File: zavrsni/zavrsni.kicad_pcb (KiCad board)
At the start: 2 copper layers, 48 parts, among them Q1 BC337, Q2 PNP, SW1 RotaryEncoder_Switch, SW2 SW_Push_DPDT, U1 PCM3060, U2 WeAct STM32F411CEU6 v3.0, U3 NE5532, U4 TL074, U5 LM358, U6 LM317_TO-220, U7 UC1609C LCD Board

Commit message: PCB design, implement basic DAC/ADC
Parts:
- removed C16: 10u, Capacitor_THT:CP_Radial_D5.0mm_P2.50mm
- removed C17: 100n, Capacitor_THT:C_Disc_D5.0mm_W2.5mm_P5.00mm
- removed SW2: SW_Push_DPDT, Button_Switch_THT:SW_Push_2P2T_Toggle_CK_PVA2xxH2xxxxxxV2
- added C18: 100n, Capacitor_THT:C_Disc_D5.0mm_W2.5mm_P5.00mm, F.Cu at (73.5, 86.0)
- added C19: 10u, Capacitor_THT:CP_Radial_D5.0mm_P2.50mm, F.Cu at (70.2, 87.0)
- added C20: 100u, Capacitor_THT:CP_Radial_D5.0mm_P2.50mm, F.Cu at (72.5, 83.2)
- added C21: 100n, Capacitor_THT:C_Disc_D5.0mm_W2.5mm_P5.00mm, F.Cu at (135.3, 108.2)
- added C22: 10u, Capacitor_THT:CP_Radial_D5.0mm_P2.50mm, F.Cu at (135.4, 91.2)
- added C23: 10u, Capacitor_THT:CP_Radial_D5.0mm_P2.50mm, F.Cu at (124.9, 70.0)
- added C24: 10u, Capacitor_THT:CP_Radial_D5.0mm_P2.50mm, F.Cu at (120.1, 95.3)
- added Jout1: Conn_01x01_Pin, Connector_Wire:SolderWirePad_1x01_SMD_4x8mm, F.Cu at (230.6, 112.3)
- added Jvcc1: Conn_01x01_Pin, Connector_Wire:SolderWirePad_1x01_SMD_4x8mm, F.Cu at (118.6, 91.0)
- added Jvss1: Conn_01x01_Pin, Connector_Wire:SolderWirePad_1x01_SMD_4x8mm, F.Cu at (146.0, 100.3)
- added SW_PRESET_0: SW_Push, Button_Switch_THT:SW_PUSH_6mm_H13mm, F.Cu at (55.0, 20.0)
- added SW_PRESET_1: SW_Push, Button_Switch_THT:SW_PUSH_6mm_H13mm, F.Cu at (55.0, 45.0)
- added SW_PRESET_2: SW_Push, Button_Switch_THT:SW_PUSH_6mm_H13mm, F.Cu at (55.0, 70.0)
- added SW_PRESET_3: SW_Push, Button_Switch_THT:SW_PUSH_6mm_H13mm, F.Cu at (55.0, 95.0)
- added SW_PRESET_4: SW_Push, Button_Switch_THT:SW_PUSH_6mm_H13mm, F.Cu at (30.0, 20.0)
- added SW_PRESET_5: SW_Push, Button_Switch_THT:SW_PUSH_6mm_H13mm, F.Cu at (30.0, 45.0)
- added SW_PRESET_6: SW_Push, Button_Switch_THT:SW_PUSH_6mm_H13mm, F.Cu at (30.0, 70.0)
- added SW_PRESET_7: SW_Push, Button_Switch_THT:SW_PUSH_6mm_H13mm, F.Cu at (30.0, 95.0)
- C12, C3: value 10u -> 100n; footprint Capacitor_THT:CP_Radial_D5.0mm_P2.50mm -> Capacitor_THT:C_Disc_D5.0mm_W2.5mm_P5.00mm
- C4: value 100n -> 10u; footprint Capacitor_THT:C_Disc_D5.0mm_W2.5mm_P5.00mm -> Capacitor_THT:CP_Radial_D5.0mm_P2.50mm
- Jin1: footprint Connector_Wire:SolderWirePad_1x01_SMD_3x6mm -> Connector_Wire:SolderWirePad_1x01_SMD_4x8mm
- Q2: value PNP -> BC317
- SW1: value RotaryEncoder_Switch -> EC11_SW; footprint Rotary_Encoder:RotaryEncoder_Alps_EC11E-Switch_Vertical_H20mm_CircularMountingHoles -> ljepi:ec11
- U1: value PCM3060 -> CS4335; footprint Package_DIP:DIP-28_W15.24mm_Socket -> Package_SO:SOIC-8_3.9x4.9mm_P1.27mm
- moved C13 155.9 mm to (264.0, 41.0)
- moved U1 147.3 mm to (270.2, 60.7)
- moved C3 138.5 mm to (254.7, 66.8)
- moved C12 138.4 mm to (254.7, 83.0)
- moved SW1 122.7 mm to (245.4, 110.3)
- moved C4 107.0 mm to (257.3, 47.5)
- moved C14 106.6 mm to (53.9, 122.8)
- moved C9 103.3 mm to (247.1, 88.6)
- moved U7 87.6 mm to (77.8, 125.0)
- moved U6 69.1 mm to (90.5, 92.5)
- moved U4 66.6 mm to (99.0, 80.5), turned to 90 degrees
- moved R3 65.1 mm to (138.6, 105.7), turned to 90 degrees
- moved R1 64.6 mm to (144.5, 84.0), turned to 90 degrees
- moved R4 62.0 mm to (141.9, 95.5), turned to -90 degrees
- moved R2 56.5 mm to (138.6, 56.9), turned to -90 degrees
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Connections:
- net IN renamed /IN
- net Net-(U2-A5) renamed /LCD_SCK
- net Net-(U2-A7) renamed /LCD_SDA
- net Net-(U2-B0) renamed /LCD_CS
- net Net-(U2-B1) renamed /LCD_CD
- C12 pad 1: +5V -> /LCD_VCC
- C13 pad 1: +3V3 -> /LCD_VCC
- C14 pad 1: GNDREF -> +12V
- C14 pad 2: +3V3 -> GNDREF
- C15 pad 1: GNDREF -> Net-(U4B-+)
- C15 pad 2: +5V -> GNDREF
- C3 pad 1: +12V -> +5V
- C3 pad 2: +0V -> GNDREF
- C4 pad 1: +12V -> +5V
- C4 pad 2: +0V -> GNDREF
- R10 pad 1: Net-(U4A-+) -> Net-(U4B-+)
- R11 pad 2: Net-(U4A-+) -> Net-(U4B-+)
- R12 pad 1: Net-(U4A--) -> Net-(U4B--)
- R13 pad 2: Net-(U4A--) -> Net-(U4B--)
- SW1 pad A: unconnected-(SW1-PadA) -> /ROT_A
- SW1 pad B: unconnected-(SW1-PadB) -> /ROT_B
- SW1 pad C: unconnected-(SW1-PadC) -> GNDREF
- SW1 pad MP: (no net) -> GNDREF
- SW1 pad S1: unconnected-(SW1-PadS1) -> /ROT_SW
- SW1 pad S2: unconnected-(SW1-PadS2) -> GNDREF
- U1 pad 1: unconnected-(U1-MC/SCL/FMT-Pad1) -> /DAC_DAT
- U1 pad 2: unconnected-(U1-MD/SDA/DEMP-Pad2) -> /DAC_BCLK
- U1 pad 3: unconnected-(U1-DOUT-Pad3) -> /DAC_LRCLK
- U1 pad 4: unconnected-(U1-LRCK1-Pad4) -> /DAC_MCLK
- U1 pad 5: unconnected-(U1-BCK1-Pad5) -> /OUT
- U1 pad 6: unconnected-(U1-SCKI1-Pad6) -> GNDREF
- U1 pad 7: +3V3 -> +5V
- U1 pad 8: GNDREF -> unconnected-(U1-AOUTL-Pad8)
- U2 pad 1: unconnected-(U2-B12-Pad1) -> /DAC_LRCLK
- U2 pad 10: unconnected-(U2-A15-Pad10) -> /PRESET6
- U2 pad 11: unconnected-(U2-B3-Pad11) -> /PRESET5
- U2 pad 12: unconnected-(U2-B4-Pad12) -> /PRESET4
- U2 pad 13: unconnected-(U2-B5-Pad13) -> /PRESET3
- U2 pad 14: unconnected-(U2-B6-Pad14) -> /PRESET2
- U2 pad 15: unconnected-(U2-B7-Pad15) -> /PRESET1
- U2 pad 17: unconnected-(U2-B9-Pad17) -> /PRESET0
- U2 pad 18: unconnected-(U2-5V-Pad18) -> +5V
- U2 pad 19: unconnected-(U2-GND-Pad19) -> GNDREF
- U2 pad 2: unconnected-(U2-B13-Pad2) -> /ROT_B
- U2 pad 20: unconnected-(U2-3V3-Pad20) -> +3V3
- U2 pad 26: unconnected-(U2-A0-Pad26) -> /ADC_IN
- U2 pad 29: unconnected-(U2-A3-Pad29) -> /DAC_MCLK
- U2 pad 3: unconnected-(U2-B14-Pad3) -> /ROT_A
- U2 pad 32: unconnected-(U2-A6-Pad32) -> /LCD_RST
- U2 pad 36: Net-(U2-B2) -> /LCD_VCC
- U2 pad 37: Net-(U2-B10) -> /DAC_BCLK
- U2 pad 39: unconnected-(U2-GND-Pad39) -> GNDREF
- U2 pad 4: unconnected-(U2-B15-Pad4) -> /DAC_DAT
- U2 pad 5: unconnected-(U2-A8-Pad5) -> /ROT_SW
- U2 pad 9: unconnected-(U2-A12-Pad9) -> /PRESET7
- U4 pad 1: Net-(R13-Pad1) -> Net-(D2-A)
- U4 pad 10: +5V -> GNDREF
- U4 pad 13: Net-(U1-V_{IN}L) -> /ADC_IN
- U4 pad 14: Net-(U1-V_{IN}L) -> /ADC_IN
- U4 pad 2: Net-(U4A--) -> Net-(D1-A)
- U4 pad 3: Net-(U4A-+) -> +5V
- U4 pad 5: GNDREF -> Net-(U4B-+)
- U4 pad 6: Net-(D1-A) -> Net-(U4B--)
- U4 pad 7: Net-(D1-K) -> Net-(R13-Pad1)
- U4 pad 8: Net-(D2-A) -> Net-(D1-K)
- U7 pad 4: Net-(U2-B2) -> /LCD_VCC
- U7 pad 7: Net-(U2-B10) -> /LCD_RST
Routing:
- net +0V: track 0.00 -> 111.9 mm, vias 0 -> 2
- net +12V: track 0.00 -> 80.6 mm
- net +5V: track 0.00 -> 41.8 mm
- net Net-(D1-A): track 0.00 -> 37.4 mm
- net Net-(U4B--): track 0.00 -> 17.8 mm
- net Net-(U5A-+): track 0.00 -> 17.5 mm
- net Net-(U3B-+): track 0.00 -> 16.4 mm
- net Net-(Q1-B): track 0.00 -> 15.4 mm
- net Net-(U6-ADJ): track 0.00 -> 12.2 mm
- net GNDREF: track 0.00 -> 11.5 mm, vias 0 -> 4
- net Net-(U3B--): track 0.00 -> 11.1 mm
- net Net-(U4B-+): track 0.00 -> 11.1 mm
- net +3V3: track 0.00 -> 10.5 mm
- net /ADC_IN: track 0.00 -> 9.32 mm
- net Net-(R13-Pad1): track 0.00 -> 8.47 mm
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- added copper zone on F.Cu, net +0V
- added copper zone on F.Cu, net +12V
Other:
- board outline added: 228.6 x 139.7 mm

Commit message: PCB is done
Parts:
- removed SW1: EC11_SW, ljepi:ec11
- removed SW_PRESET_7: SW_Push, Button_Switch_THT:SW_PUSH_6mm_H13mm
- U6: footprint Package_TO_SOT_THT:TO-220-3_Vertical -> Package_TO_SOT_THT:TO-220-3_Horizontal_TabDown
- moved C9 190.9 mm to (56.7, 101.4), turned to -90 degrees
- moved SW_UP1 173.0 mm to (184.4, 98.0), turned to 90 degrees
- moved SW_DOWN1 168.8 mm to (184.4, 113.0), turned to 90 degrees
- moved C13 165.2 mm to (107.5, 93.9), turned to 90 degrees
- moved U1 155.1 mm to (115.1, 60.5), turned to 90 degrees
- moved SW_OK1 154.5 mm to (184.4, 72.0), turned to 90 degrees
- moved C4 151.6 mm to (106.5, 62.4), turned to 90 degrees
- moved C12 150.6 mm to (104.2, 88.4)
- moved C3 144.0 mm to (110.8, 62.2), turned to 90 degrees
- moved SW_PRESET_3 135.7 mm to (184.7, 134.8), turned to 90 degrees
- moved SW_PRESET_2 125.2 mm to (162.1, 134.8), turned to 90 degrees
- moved SW_PRESET_0 124.1 mm to (102.1, 134.8), turned to 90 degrees
- moved Jout1 123.1 mm to (120.2, 57.9)
- moved SW_PRESET_1 118.4 mm to (132.1, 134.8), turned to 90 degrees
- moved Jvss1 97.5 mm to (55.0, 135.3), turned to -90 degrees
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- renumbered SW_PRESET_5 to SW_DOWN1, SW_PRESET_6 to SW_OK1, SW_PRESET_4 to SW_UP1
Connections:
- net /PRESET0 renamed /BTN_PRESET0
- net /PRESET1 renamed /BTN_PRESET1
- net /PRESET2 renamed /BTN_PRESET2
- net /PRESET3 renamed /BTN_PRESET3
- net /PRESET6 renamed /BTN_OK
- SW_DOWN1 pad 1: /PRESET5 -> /BTN_DOWN
- SW_UP1 pad 1: /PRESET4 -> /BTN_UP
- U2 pad 11: /PRESET5 -> /BTN_UP
- U2 pad 12: /PRESET4 -> /BTN_DOWN
- U2 pad 2: /ROT_B -> /DAC_BCLK
- U2 pad 3: /ROT_A -> unconnected-(U2-B14-Pad3)
- U2 pad 37: /DAC_BCLK -> unconnected-(U2-B10-Pad37)
- U2 pad 38: unconnected-(U2-3V3-Pad38) -> +3V3
- U2 pad 5: /ROT_SW -> unconnected-(U2-A8-Pad5)
- U2 pad 9: /PRESET7 -> unconnected-(U2-A12-Pad9)
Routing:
- net /BTN_PRESET3: track 0.00 -> 145.4 mm
- net /BTN_PRESET2: track 0.00 -> 125.7 mm
- net /BTN_DOWN: track 0.00 -> 117.2 mm
- net /BTN_PRESET0: track 0.00 -> 115.8 mm
- net /BTN_UP: track 0.00 -> 108.2 mm
- net /BTN_PRESET1: track 0.00 -> 99.3 mm
- net /BTN_OK: track 0.00 -> 91.8 mm
- net /LCD_SCK: track 0.00 -> 68.2 mm
- net +5V: track 41.8 -> 97.5 mm
- net /LCD_SDA: track 0.00 -> 54.9 mm
- net /DAC_MCLK: track 0.00 -> 46.1 mm, vias 0 -> 1
- net /LCD_RST: track 0.00 -> 35.2 mm, vias 0 -> 2
- net /LCD_CS: track 0.00 -> 34.0 mm
- net /LCD_CD: track 0.00 -> 30.0 mm
- net +12V: track 80.6 -> 107.6 mm
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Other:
- board size 228.6 x 139.7 mm -> 156.4 x 99.2 mm
- board text added: "${CRTAO} Pedala multiefekata za električnu gitaru ${DATUM} v${VERZIJA}"

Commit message: PCB prototype finishing touches
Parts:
- removed C10: 100n, Capacitor_THT:C_Disc_D5.0mm_W2.5mm_P5.00mm
- removed C23: 10u, Capacitor_THT:CP_Radial_D5.0mm_P2.50mm
- removed R5: 1k, Resistor_THT:R_Axial_DIN0207_L6.3mm_D2.5mm_P10.16mm_Horizontal
- added RV1: R_Potentiometer_MountingPin, ljepi:pot vertikalni 5 pin, F.Cu at (70.9, 120.9)
- added SW_TUNER1: SW_Push, Button_Switch_THT:SW_PUSH_6mm_H13mm, F.Cu at (95.2, 116.0)
- D1, D2: footprint Diode_THT:D_DO-35_SOD27_P7.62mm_Horizontal -> Diode_THT:D_DO-35_SOD27_P2.54mm_Vertical_AnodeUp
- Q2: value BC317 -> BC327
- R1, R10, R12, R9: footprint Resistor_THT:R_Axial_DIN0207_L6.3mm_D2.5mm_P10.16mm_Horizontal -> Resistor_THT:R_Axial_DIN0207_L6.3mm_D2.5mm_P5.08mm_Vertical
- R11, R13, R2, R7, R8: footprint Resistor_THT:R_Axial_DIN0207_L6.3mm_D2.5mm_P10.16mm_Horizontal -> Resistor_THT:R_Axial_DIN0207_L6.3mm_D2.5mm_P2.54mm_Vertical
- R6: value 330 -> 300; footprint Resistor_THT:R_Axial_DIN0207_L6.3mm_D2.5mm_P10.16mm_Horizontal -> Resistor_THT:R_Axial_DIN0207_L6.3mm_D2.5mm_P2.54mm_Vertical
- moved SW_UP1 65.7 mm to (121.2, 116.0), turned to -90 degrees
- moved SW_OK1 52.9 mm to (168.8, 122.5)
- moved SW_DOWN1 42.8 mm to (142.8, 122.5)
- moved SW_PRESET_2 19.6 mm to (142.8, 138.2)
- moved SW_PRESET_3 16.3 mm to (168.8, 138.2)
- moved C7 15.5 mm to (82.6, 120.9)
- moved SW_PRESET_1 11.3 mm to (121.2, 131.8), turned to -90 degrees
- moved R7 9.25 mm to (55.8, 91.5)
- moved D1 9.20 mm to (85.2, 103.6), turned to 90 degrees
- moved R6 9.01 mm to (75.6, 123.7)
- moved R2 8.92 mm to (82.0, 142.2), turned to 0 degrees
- moved C1 8.85 mm to (78.9, 140.5), turned to -90 degrees
- moved C2 7.83 mm to (81.7, 137.9), turned to 0 degrees
- moved SW_PRESET_0 7.50 mm to (95.2, 131.8), turned to -90 degrees
- moved R12 7.39 mm to (81.5, 109.7), turned to -90 degrees
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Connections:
- Q2 pad 1: GNDREF -> +0V
- Q2 pad 3: +0V -> GNDREF
- U2 pad 11: /BTN_UP -> /BTN_DOWN
- U2 pad 12: /BTN_DOWN -> /BTN_PRESET3
- U2 pad 13: /BTN_PRESET3 -> /BTN_PRESET2
- U2 pad 14: /BTN_PRESET2 -> /BTN_PRESET1
- U2 pad 15: /BTN_PRESET1 -> /BTN_PRESET0
- U2 pad 16: unconnected-(U2-B8-Pad16) -> /BTN_UP
- U2 pad 17: /BTN_PRESET0 -> /BTN_TUNER
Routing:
- net /BTN_TUNER: track 0.00 -> 121.6 mm, vias 0 -> 2
- net +12V: track 107.6 -> 79.6 mm
- net /BTN_DOWN: track 117.2 -> 91.1 mm, vias 0 -> 2
- net GNDREF: track 27.0 -> 4.06 mm, vias 6 -> 2
- net /BTN_OK: track 91.8 -> 114.5 mm, vias 0 -> 2
- net /BTN_PRESET0: track 115.8 -> 137.2 mm, vias 0 -> 2
- net Net-(C7-Pad1): track 7.10 -> 21.1 mm
- net /BTN_PRESET2: track 125.7 -> 111.8 mm, vias 0 -> 2
- net /BTN_UP: track 108.2 -> 95.6 mm, vias 0 -> 2
- net /BTN_PRESET1: track 99.3 -> 111.1 mm, vias 0 -> 2
- net /BTN_PRESET3: track 145.4 -> 135.3 mm, vias 0 -> 2
- net Net-(D1-K): track 8.14 -> 2.84 mm
- net Net-(U3B--): track 11.6 -> 7.88 mm
- net Net-(U3B-+): track 17.9 -> 20.8 mm
- net /OUT: track 3.96 -> 6.33 mm
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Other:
- board size 156.4 x 99.2 mm -> 149.4 x 96.2 mm
- board text added: "${CRTAO} Mutliefekt pedala za električnu gitaru ${DATUM} v${VERZIJA}"
- board text removed: "${CRTAO} Pedala multiefekata za električnu gitaru ${DATUM} v${VERZIJA}"

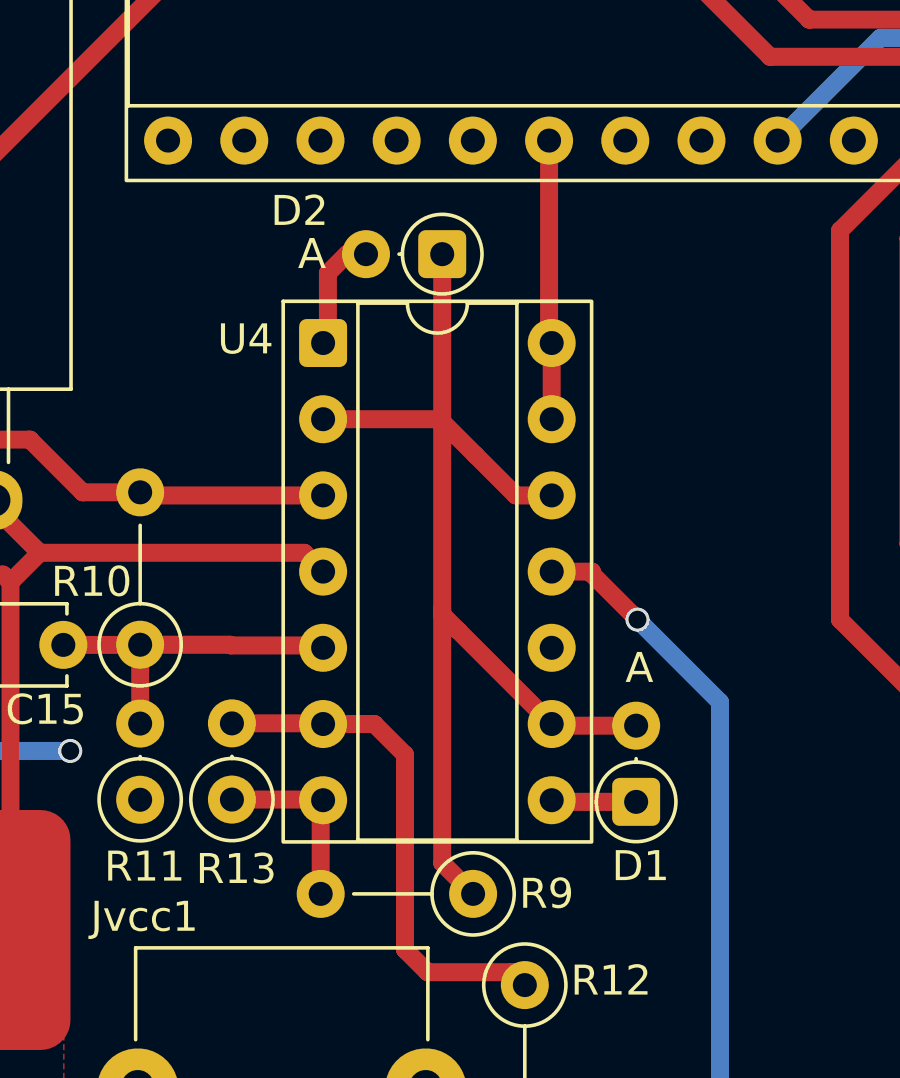
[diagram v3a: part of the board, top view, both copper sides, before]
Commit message: izbrisi svg pdfove, zamjeni polaritet 2 diode
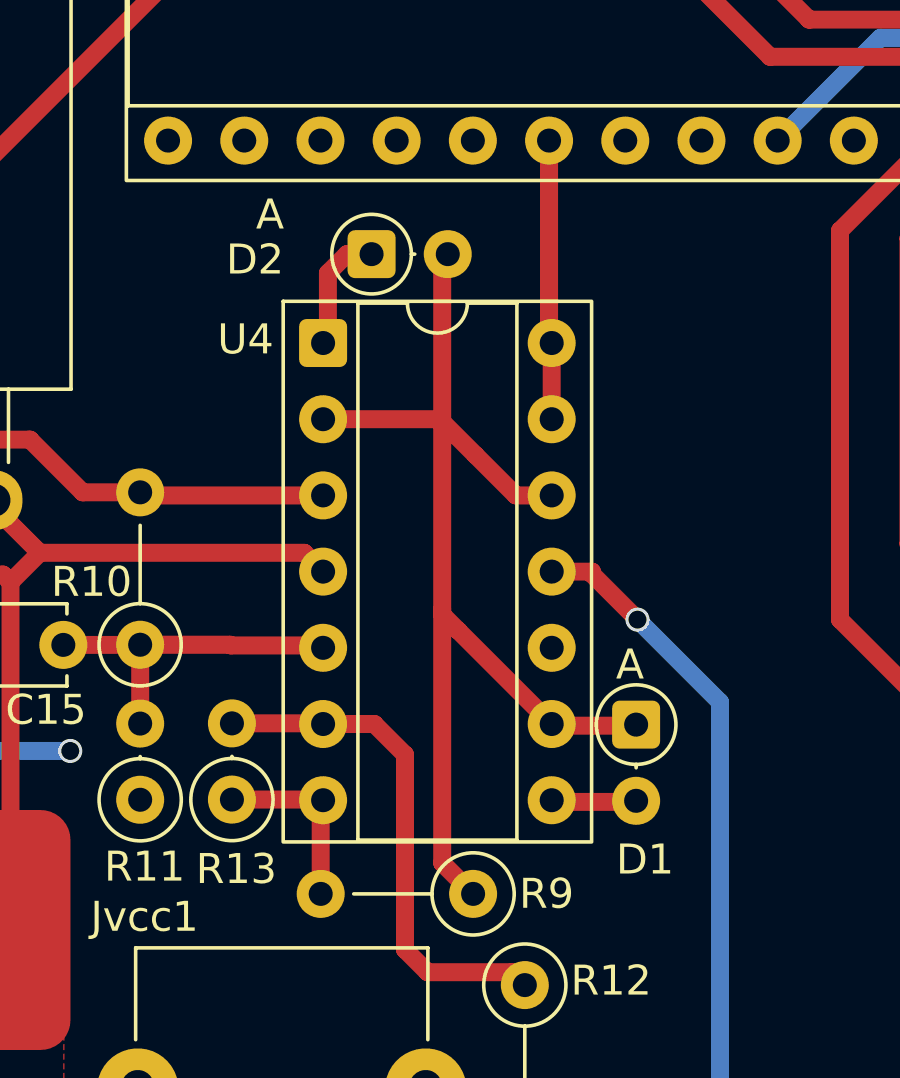
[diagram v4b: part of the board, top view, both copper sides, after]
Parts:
- moved D1 2.58 mm to (85.2, 101.0), turned to -90 degrees
- moved D2 2.35 mm to (76.4, 85.3), turned to 0 degrees
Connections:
- D2 pad 1: Net-(D1-A) -> Net-(D2-K)
- D2 pad 2: Net-(D2-A) -> Net-(D1-K)
- R9 pad 1: Net-(D1-A) -> Net-(D1-K)
- U4 pad 1: Net-(D2-A) -> Net-(D2-K)
- U4 pad 12: Net-(D1-A) -> Net-(D1-K)
- U4 pad 2: Net-(D1-A) -> Net-(D1-K)
- U4 pad 8: Net-(D1-K) -> Net-(D1-A)
- U4 pad 9: Net-(D1-A) -> Net-(D1-K)
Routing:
- net Net-(D1-K): track 2.84 -> 38.9 mm
- net Net-(D1-A): track 38.9 -> 2.84 mm
- net Net-(D2-K): track 0.00 -> 3.93 mm
- net Net-(D2-A): track 3.93 -> 0.00 mm
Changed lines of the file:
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@@
 	(net 28 "Net-(D1-K)")
 	(net 29 "Net-(D1-A)")
-	(net 30 "Net-(D2-A)")
+	(net 30 "Net-(D2-K)")
 	(net 31 "Net-(Q1-B)")
 	(net 32 "Net-(U3A--)")
@@
 	(footprint "Diode_THT:D_DO-35_SOD27_P2.54mm_Vertical_AnodeUp"
 		(layer "F.Cu")
-		(at 85.204646 103.575538 90)
+		(at 85.204646 101 -90)
 		(descr "Diode, DO-35_SOD27 series, Axial, Vertical, pin pitch=2.54mm, length*diameter=4*2mm^2, http://www.diodes.com/_files/packages/DO-35.pdf")
 		(tags "Diode DO-35_SOD27 series Axial Vertical pin pitch 2.54mm  length 4mm diameter 2mm")
 		(property "Reference" "D1"
-			(at -2.145133 0.152333 180)
+			(at 4.5 -0.295354 0)
 			(layer "F.SilkS")
 			(effects
@@
 		)
 		(property "Sim.Device" "D"
-			(at 0 0 90)
+			(at 0 0 270)
 			(unlocked yes)
 			(layer "F.Fab")
@@
 		)
 		(property "Sim.Pins" "1=K 2=A"
-			(at 0 0 90)
+			(at 0 0 270)
 			(unlocked yes)
 			(layer "F.Fab")
@@
 		)
 		(fp_text user "A"
-			(at 4.460235 0.109066 180)
+			(at -2 0.204646 0)
 			(layer "F.SilkS")
 			(effects
@@
 		)
 		(pad "1" thru_hole roundrect
-			(at 0 0 90)
+			(at 0 0 270)
 			(size 1.6 1.6)
 			(drill 0.8)
@@
 		)
 		(pad "2" thru_hole circle
-			(at 2.54 0 90)
+			(at 2.54 0 270)
 			(size 1.6 1.6)
 			(drill 0.8)
@@
 			(remove_unused_layers no)
 			(roundrect_rratio 0.15625)
-			(net 30 "Net-(D2-A)")
+			(net 30 "Net-(D2-K)")
 			(pintype "output")
 		)
@@
 			(layers "*.Cu" "*.Mask")
 			(remove_unused_layers no)
-			(net 29 "Net-(D1-A)")
+			(net 28 "Net-(D1-K)")
 			(pinfunction "-")
 			(pintype "input")
@@
 			(layers "*.Cu" "*.Mask")
 			(remove_unused_layers no)
-			(net 28 "Net-(D1-K)")
+			(net 29 "Net-(D1-A)")
 			(pintype "output")
 		)
@@
 			(layers "*.Cu" "*.Mask")
 			(remove_unused_layers no)
-			(net 29 "Net-(D1-A)")
+			(net 28 "Net-(D1-K)")
 			(pinfunction "-")
 			(pintype "input")
@@
 			(layers "*.Cu" "*.Mask")
 			(remove_unused_layers no)
-			(net 29 "Net-(D1-A)")
+			(net 28 "Net-(D1-K)")
 			(pinfunction "+")
 			(pintype "input")
@@
 			(layers "*.Cu" "*.Mask")
 			(remove_unused_layers no)
-			(net 29 "Net-(D1-A)")
+			(net 28 "Net-(D1-K)")
 			(pintype "passive")
 		)
@@
 	(footprint "Diode_THT:D_DO-35_SOD27_P2.54mm_Vertical_AnodeUp"
 		(layer "F.Cu")
-		(at 78.74 85.317774 180)
+		(at 76.385686 85.317774)
 		(descr "Diode, DO-35_SOD27 series, Axial, Vertical, pin pitch=2.54mm, length*diameter=4*2mm^2, http://www.diodes.com/_files/packages/DO-35.pdf")
 		(tags "Diode DO-35_SOD27 series Axial Vertical pin pitch 2.54mm  length 4mm diameter 2mm")
 		(property "Reference" "D2"
-			(at 4.755173 1.43664 180)
+			(at -3.885686 0.182226 0)
 			(layer "F.SilkS")
 			(effects
@@
 		)
 		(property "Value" "1N4148"
-			(at 1.27 3.215371 180)
+			(at 1.27 3.215371 0)
 			(layer "F.Fab")
 			(effects
@@
 		)
 		(property "Datasheet" "https://assets.nexperia.com/documents/data-sheet/1N4148_1N4448.pdf"
-			(at 0 0 180)
+			(at 0 0 0)
 			(layer "F.Fab")
 			(hide yes)
@@
 		)
 		(property "Description" "100V 0.15A standard switching diode, DO-35"
-			(at 0 0 180)
+			(at 0 0 0)
 			(layer "F.Fab")
 			(hide yes)
@@
 		)
 		(property "Sim.Device" "D"
-			(at 0 0 180)
+			(at 0 0 0)
 			(unlocked yes)
 			(layer "F.Fab")
@@
 		)
 		(property "Sim.Pins" "1=K 2=A"
-			(at 0 0 180)
+			(at 0 0 0)
 			(unlocked yes)
 			(layer "F.Fab")
@@
 		)
 		(fp_text user "A"
-			(at 4.34 0 180)
+			(at -3.385686 -1.317774 0)
 			(layer "F.SilkS")
 			(effects
@@
 		)
 		(fp_text user "${REFERENCE}"
-			(at 4.755173 1.43664 180)
+			(at 4.755173 1.43664 0)
 			(layer "F.Fab")
 			(effects
@@
 		)
 		(fp_text user "A"
-			(at 4.34 0 180)
+			(at 4.34 0 0)
 			(layer "F.Fab")
 			(effects
@@
 		)
 		(pad "1" thru_hole roundrect
-			(at 0 0 180)
+			(at 0 0)
 			(size 1.6 1.6)
 			(drill 0.8)
@@
 			(remove_unused_layers no)
 			(roundrect_rratio 0.15625)
-			(net 29 "Net-(D1-A)")
+			(net 30 "Net-(D2-K)")
 			(pinfunction "K")
 			(pintype "passive")
 		)
 		(pad "2" thru_hole circle
-			(at 2.54 0 180)
+			(at 2.54 0)
 			(size 1.6 1.6)
 			(drill 0.8)
 			(layers "*.Cu" "*.Mask")
 			(remove_unused_layers no)
-			(net 30 "Net-(D2-A)")
+			(net 28 "Net-(D1-K)")
 			(pinfunction "A")
 			(pintype "passive")
@@
 	)
 	(segment
-		(start 82.445538 103.575538)
-		(end 82.39 103.52)
-		(width 0.6)
-		(layer "F.Cu")
-		(net 28)
-	)
-	(segment
-		(start 85.204646 103.575538)
-		(end 82.445538 103.575538)
-		(width 0.6)
-		(layer "F.Cu")
-		(net 28)
-	)
-	(segment
 		(start 80.01 106.402585)
 		(end 79.77 106.642585)
 		(width 0.6)
 		(layer "F.Cu")
-		(net 29)
+		(net 28)
 	)
 	(segment
@@
 		(width 0.6)
 		(layer "F.Cu")
-		(net 29)
+		(net 28)
 	)
 	(segment
@@
 		(width 0.6)
 		(layer "F.Cu")
-		(net 29)
+		(net 28)
 	)
 	(segment
@@
 		(width 0.6)
 		(layer "F.Cu")
-		(net 29)
+		(net 28)
 	)
 	(segment
@@
 		(width 0.6)
 		(layer "F.Cu")
-		(net 29)
+		(net 28)
 	)
 	(segment
@@
 		(width 0.6)
 		(layer "F.Cu")
-		(net 29)
+		(net 28)
 	)
 	(segment
@@
 		(width 0.6)
 		(layer "F.Cu")
-		(net 29)
+		(net 28)
 	)
 	(segment
@@
 		(width 0.6)
 		(layer "F.Cu")
-		(net 29)
+		(net 28)
 	)
 	(segment
@@
 		(width 0.6)
 		(layer "F.Cu")
-		(net 29)
+		(net 28)
 	)
 	(segment
@@
 		(width 0.6)
 		(layer "F.Cu")
-		(net 29)
+		(net 28)
 	)
 	(segment
@@
 		(width 0.6)
 		(layer "F.Cu")
-		(net 29)
+		(net 28)
 	)
 	(segment
@@
 		(width 0.6)
 		(layer "F.Cu")
-		(net 29)
+		(net 28)
 	)
 	(segment
@@
 		(width 0.6)
 		(layer "F.Cu")
-		(net 29)
+		(net 28)
 	)
 	(segment
@@
 		(width 0.6)
 		(layer "F.Cu")
+		(net 28)
+	)
+	(segment
+		(start 82.445538 103.575538)
+		(end 82.39 103.52)
+		(width 0.6)
+		(layer "F.Cu")
+		(net 29)
+	)
+	(segment
+		(start 85.204646 103.575538)
+		(end 82.445538 103.575538)
+		(width 0.6)
+		(layer "F.Cu")
